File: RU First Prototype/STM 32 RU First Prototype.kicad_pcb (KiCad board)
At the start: 4 copper layers, 44.5 x 76.5 mm, 98 parts, among them J1 Conn_01x02, J10 Conn_01x02_Pin, J11 Conn_01x02_Pin, J12 1776113-2, J2 USB_C_Receptacle, J3 Conn_01x02_Pin, J4 Conn_01x04, J5 Conn_01x02_Pin, J7 1776113-2, J9 Conn_01x02_Pin, Q1 SISA96DN-T1, Q3 SISA96DN-T1, SW1 SW_SPDT, U1 STM32F412RGTx, U2 AMS1117-3.3, U3 MS5611, U4 KX134-1211, U5 W25Q16JVSS, U6 TCAN330, U7 TCAN330, Y1 Crystal_8Mhz

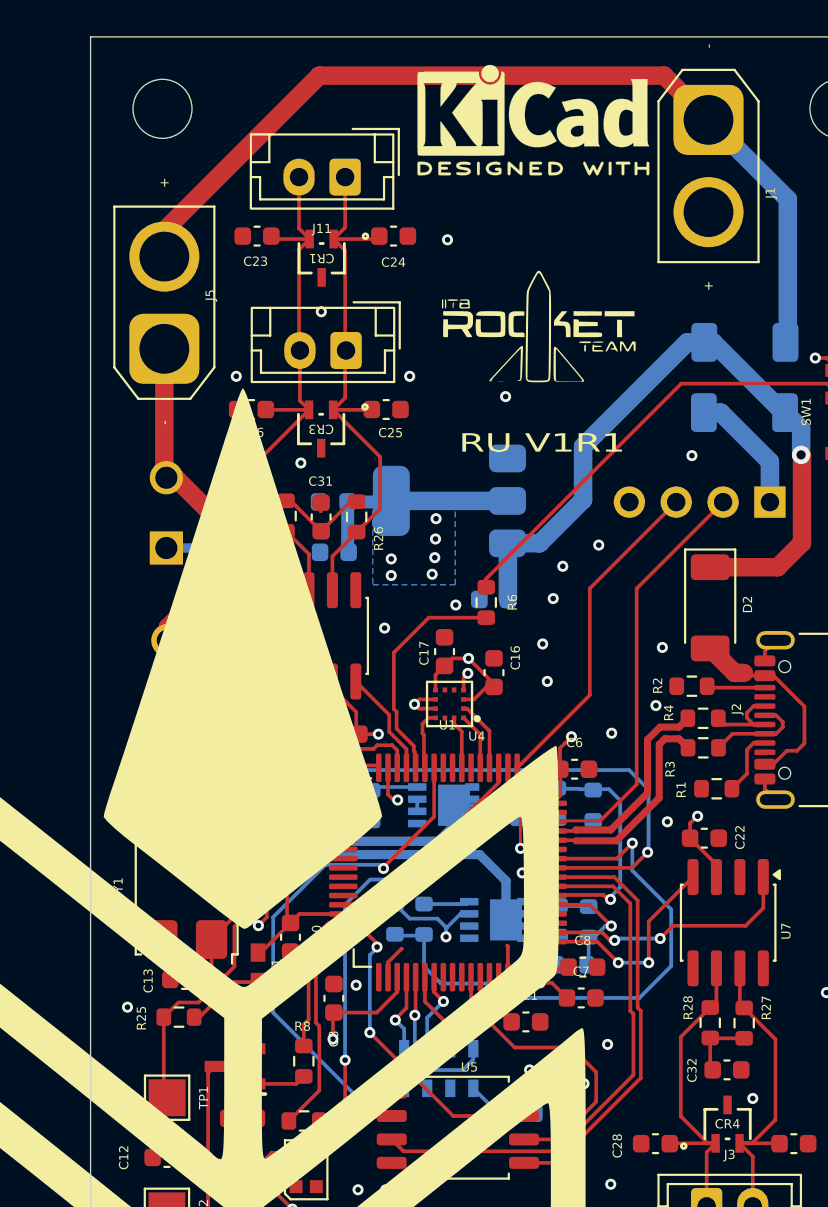
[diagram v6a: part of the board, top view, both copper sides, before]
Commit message: Fixed SDO-SDI, Added Battery monitoring, and ADC inputs
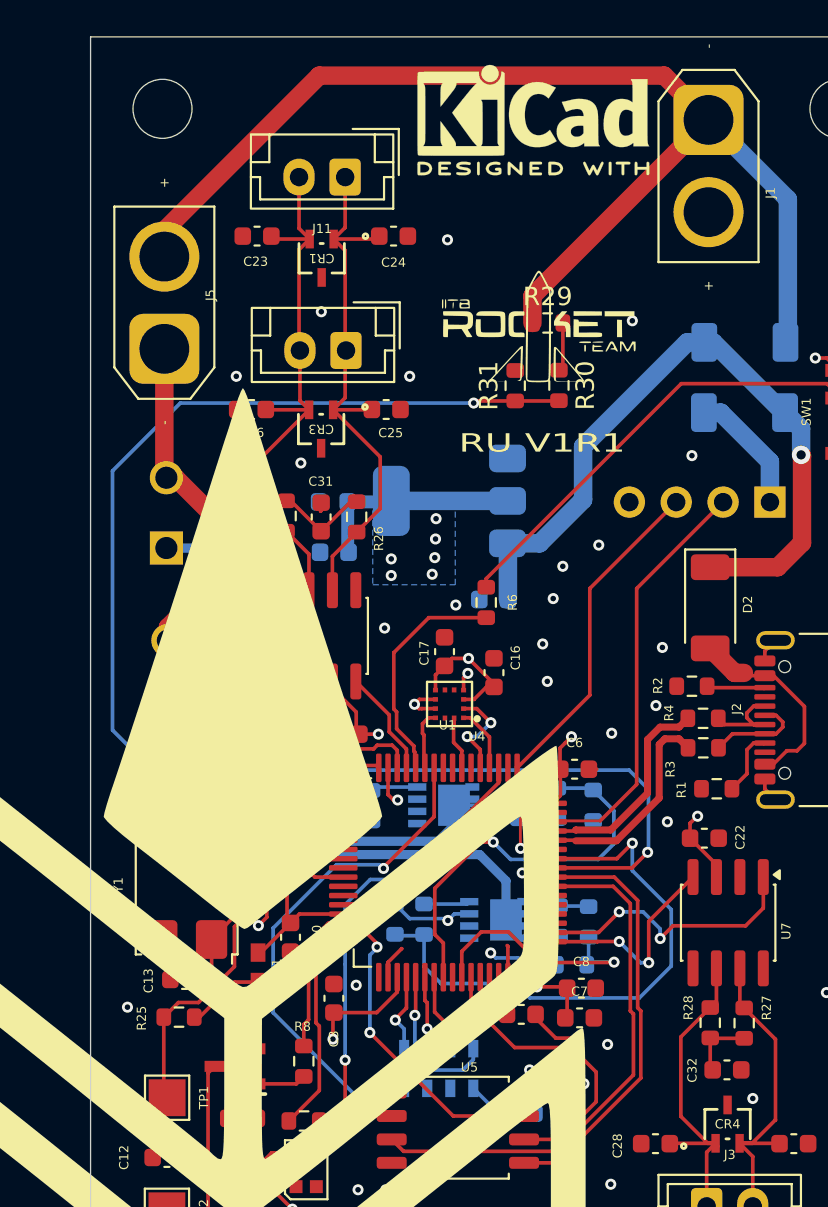
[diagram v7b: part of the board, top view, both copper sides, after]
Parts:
- added R29: 10k, Resistor_SMD:R_0603_1608Metric, F.Cu at (126.8, 70.0)
- added R30: 10k, Resistor_SMD:R_0603_1608Metric, F.Cu at (127.4, 73.4)
- added R31: 13k, Resistor_SMD:R_0603_1608Metric, F.Cu at (125.0, 73.4)
- moved C8 1.14 mm to (128.6, 106.1)
- moved C7 1.08 mm to (128.5, 107.7)
- moved C11 0.48 mm to (125.3, 107.5)
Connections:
- R19 pad 2: /PC7 -> /Main_Sense
- R20 pad 1: /PC7 -> /Main_Sense
- R22 pad 2: /PC6 -> /Drogue_Sense
- R23 pad 1: /PC6 -> /Drogue_Sense
- U1 pad 22: /ALT_SDI -> /ALT_SDO
- U1 pad 23: /ALT_SDO -> /ALT_SDI
- U1 pad 24: unconnected-(U1-PC4-Pad24) -> /Main_Sense
- U1 pad 26: unconnected-(U1-PB0-Pad26) -> /Drogue_Sense
- U1 pad 37: /PC6 -> unconnected-(U1-PC6-Pad37)
- U1 pad 38: /PC7 -> unconnected-(U1-PC7-Pad38)
- U1 pad 52: /KX_SDI -> /KX_SDO
- U1 pad 53: /KX_SDO -> /KX_SDI
- U1 pad 9: unconnected-(U1-PC1-Pad9) -> /Bat_Sense
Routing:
- net /Bat_Sense: track 0.00 -> 56.7 mm, vias 0 -> 2
- net /Main_Sense: track 0.00 -> 21.9 mm, vias 0 -> 1
- net /V_2S: track 49.5 -> 64.5 mm
- net /Drogue_Sense: track 0.00 -> 13.9 mm, vias 0 -> 1
- net /PC7: track 12.7 -> 0.00 mm, vias 1 -> 0
- net /PC6: track 6.75 -> 0.00 mm, vias 1 -> 0
- net GND: track 26.0 -> 31.5 mm, vias 48 -> 49
- net Net-(R29-Pad2): track 0.00 -> 2.65 mm
- net /KX_SDI: track 3.90 -> 5.43 mm, vias 0 -> 2
- net /CAN_TX2: track 14.1 -> 15.2 mm
- net /ALT_SDO: track 4.45 -> 3.93 mm
- net Net-(U1-VCAP_1): track 2.71 -> 2.20 mm
